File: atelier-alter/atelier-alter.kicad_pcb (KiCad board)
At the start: 2 copper layers, 71.4 x 99.5 mm, 28 parts, among them SW1 SW_Push, U1 ATmega32U4-A, Y1 16Mhz

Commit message: redrawn
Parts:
- added Alter: LOGO, Alter_Drawing, F.Cu at (126.2, 120.7)
- added C10: 100nF, Capacitor_SMD:C_0805_2012Metric, B.Cu at (161.3, 132.6)
- added C11: 100nF, Capacitor_SMD:C_0805_2012Metric, B.Cu at (168.9, 122.1)
- added C8: 100nF, Capacitor_SMD:C_0805_2012Metric, B.Cu at (124.5, 109.5)
- added C9: 100nF, Capacitor_SMD:C_0805_2012Metric, B.Cu at (146.2, 68.3)
- added D10: SK6812, LED_SMD:LED_SK6812_PLCC4_5.0x5.0mm_P3.2mm, B.Cu at (153.2, 111.9)
- added D7: SK6812, LED_SMD:LED_SK6812_PLCC4_5.0x5.0mm_P3.2mm, B.Cu at (127.8, 91.3)
- added D8: SK6812, LED_SMD:LED_SK6812_PLCC4_5.0x5.0mm_P3.2mm, B.Cu at (131.0, 111.9)
- added D9: SK6812, LED_SMD:LED_SK6812_PLCC4_5.0x5.0mm_P3.2mm, B.Cu at (156.4, 91.3)
- added R5: 300, Resistor_SMD:R_0805_2012Metric, B.Cu at (122.4, 68.3)
- C1, C3, C4, C5, C6, D1, D2, D3, D4, D5, D6, R3, U1, Y1: moved to B.Cu
- C2: value C_Small -> 1uF; moved to B.Cu
- C7: value 0.1uF -> 10uF; moved to B.Cu
- R1, R2: value R_Small -> 22
- SW1: value SW_Push -> RESET; moved to B.Cu
- moved R3 52.8 mm to (169.0, 112.7), turned to -90 degrees
- moved F1 49.0 mm to (166.6, 68.3), turned to 180 degrees
- moved SW1 40.9 mm to (161.9, 111.9), turned to 180 degrees
- moved C2 33.4 mm to (161.2, 127.8), turned to 180 degrees
- moved Y1 29.3 mm to (161.6, 122.9), turned to -90 degrees
- moved C1 25.1 mm to (161.4, 118.3), turned to 180 degrees
- moved C5 19.9 mm to (146.9, 111.1), turned to 0 degrees
- moved D5 19.2 mm to (153.2, 79.4), turned to -90 degrees
- moved D1 19.2 mm to (115.1, 79.4), turned to -90 degrees
- moved D3 19.2 mm to (134.1, 79.4), turned to -90 degrees
- moved D4 19.2 mm to (134.1, 98.5), turned to -90 degrees
- moved D6 19.2 mm to (153.2, 98.4), turned to -90 degrees
- moved D2 19.2 mm to (115.1, 98.4), turned to -90 degrees
- moved C6 18.1 mm to (146.9, 113.6), turned to 0 degrees
- moved USB1 16.0 mm to (142.1, 59.8)
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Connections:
- U1 pad 11: unconnected-(U1-Pad11) -> COL1
- U1 pad 27: unconnected-(U1-Pad27) -> ROW1
- U1 pad 28: unconnected-(U1-Pad28) -> COL2
- U1 pad 29: unconnected-(U1-Pad29) -> COL3
- U1 pad 30: unconnected-(U1-Pad30) -> ROW2
- U1 pad 41: unconnected-(U1-Pad41) -> UGLOW1
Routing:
- net UGLOW1: track 0.00 -> 76.9 mm, vias 0 -> 2
- net Net-(R3-Pad1): track 88.5 -> 18.7 mm, vias 0 -> 2
- net ROW1: track 40.0 -> 101.3 mm, vias 3 -> 0
- net ROW2: track 39.8 -> 97.6 mm, vias 3 -> 4
- net COL1: track 19.1 -> 65.6 mm, vias 0 -> 2
- net Net-(D8-Pad4): track 0.00 -> 36.4 mm, vias 0 -> 2
- net Net-(R4-Pad1): track 99.2 -> 67.8 mm, vias 2 -> 3
- net COL2: track 23.9 -> 51.9 mm, vias 0 -> 4
- net Net-(D10-Pad2): track 0.00 -> 25.4 mm, vias 0 -> 2
- net Net-(D7-Pad2): track 0.00 -> 25.1 mm
- net +5V: track 201.1 -> 225.8 mm, vias 6 -> 10
- net Net-(D7-Pad4): track 0.00 -> 19.5 mm
- net Net-(R1-Pad2): track 68.3 -> 52.9 mm, vias 0 -> 1
- net COL3: track 41.9 -> 55.1 mm
- net D-: track 29.6 -> 20.9 mm
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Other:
- board size 71.4 x 99.5 mm -> 61.9 x 78.6 mm
- board text added: "Atelier_Alter_Prototype"
- board text removed: "Atelier_Alter_v0.1"

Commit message: da route thu nghiem xong xuoi
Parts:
- R5: moved to F.Cu
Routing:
- net ROW1: track 101.3 -> 141.4 mm, vias 0 -> 5
- net ROW2: track 97.6 -> 117.9 mm, vias 4 -> 6
- net COL3: track 55.1 -> 74.8 mm, vias 0 -> 2
- net +5V: track 225.8 -> 228.4 mm
- net COL2: track 51.9 -> 53.5 mm
- net Net-(R4-Pad1): track 67.8 -> 68.9 mm
- net GND: track 224.0 -> 224.9 mm
- net COL1: track 65.6 -> 66.3 mm
- net UGLOW1: track 76.9 -> 76.3 mm, vias 2 -> 1
- net Net-(D7-Pad2): vias 0 -> 1

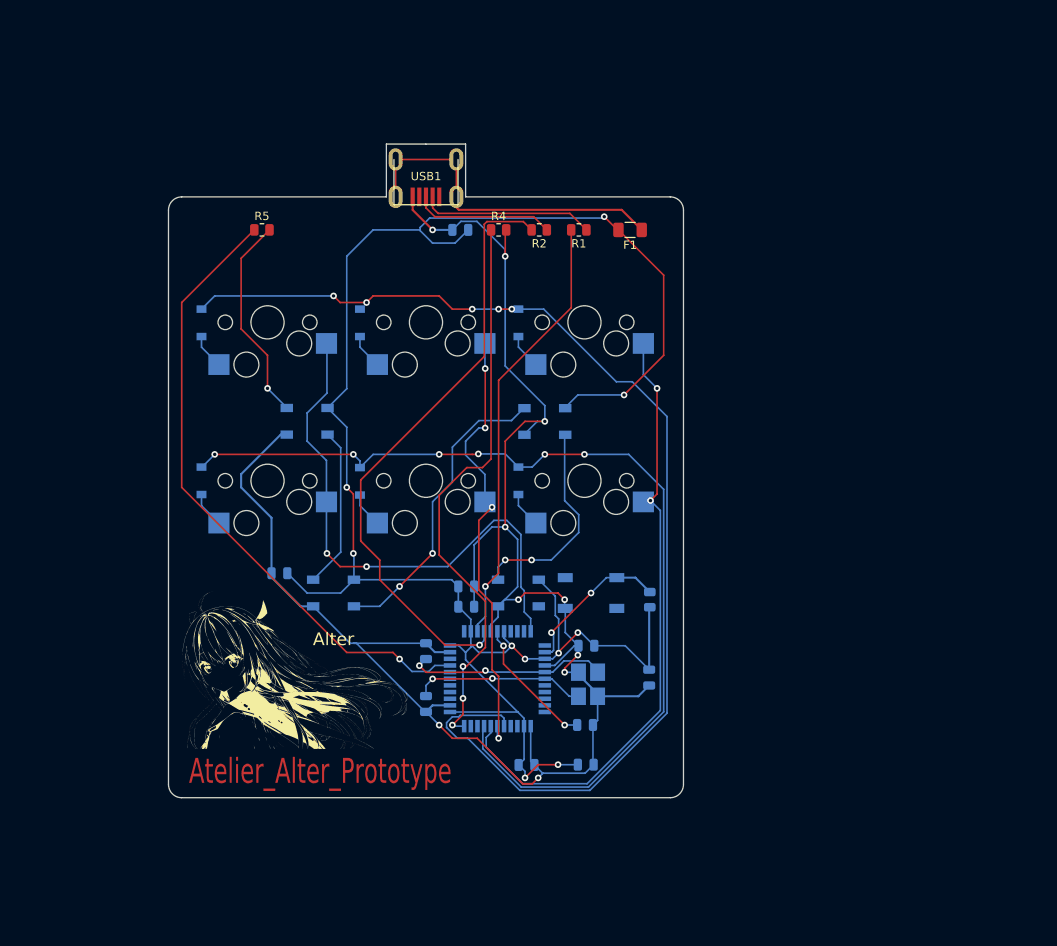
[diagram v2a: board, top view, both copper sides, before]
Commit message: redrawn lan 3, them vai chuc nang
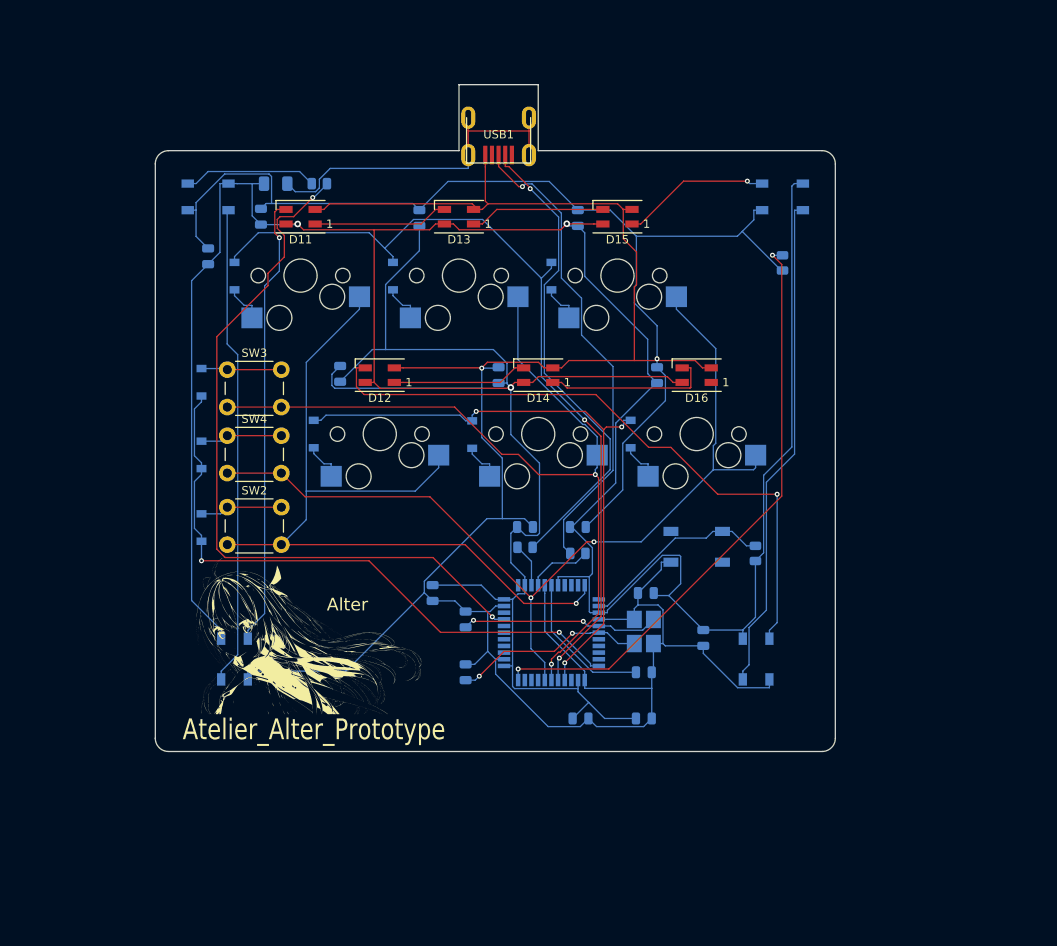
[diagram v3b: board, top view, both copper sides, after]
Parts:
- added C12: 100uF, Capacitor_SMD:C_0805_2012Metric, B.Cu at (122.2, 66.7)
- added C13: 100uF, Capacitor_SMD:C_0805_2012Metric, B.Cu at (131.8, 85.6)
- added C14: 100uF, Capacitor_SMD:C_0805_2012Metric, B.Cu at (141.3, 66.8)
- added C15: 100uF, Capacitor_SMD:C_0805_2012Metric, B.Cu at (150.8, 85.7)
- added C16: 100uF, Capacitor_SMD:C_0805_2012Metric, B.Cu at (160.3, 66.8)
- added C17: 100uF, Capacitor_SMD:C_0805_2012Metric, B.Cu at (169.9, 85.7)
- added D11: SK6812MINI, LED_SMD:LED_SK6812MINI_PLCC4_3.5x3.5mm_P1.75mm, F.Cu at (127.0, 66.7)
- added D12: SK6812MINI, LED_SMD:LED_SK6812MINI_PLCC4_3.5x3.5mm_P1.75mm, F.Cu at (136.5, 85.7)
- added D13: SK6812MINI, LED_SMD:LED_SK6812MINI_PLCC4_3.5x3.5mm_P1.75mm, F.Cu at (146.1, 66.7)
- added D14: SK6812MINI, LED_SMD:LED_SK6812MINI_PLCC4_3.5x3.5mm_P1.75mm, F.Cu at (155.6, 85.7)
- added D15: SK6812MINI, LED_SMD:LED_SK6812MINI_PLCC4_3.5x3.5mm_P1.75mm, F.Cu at (165.1, 66.7)
- added D16: SK6812MINI, LED_SMD:LED_SK6812MINI_PLCC4_3.5x3.5mm_P1.75mm, F.Cu at (174.6, 85.7)
- added D17: SOD-123, Diode_SMD:D_SOD-123, B.Cu at (115.1, 104.0)
- added D18: SOD-123, Diode_SMD:D_SOD-123, B.Cu at (115.1, 86.6)
- added D19: SOD-123, Diode_SMD:D_SOD-123, B.Cu at (115.1, 95.3)
- added SW2: SW_DPST, Button_Switch_THT:SW_PUSH_6mm_H9.5mm, F.Cu at (118.2, 101.6)
- added SW3: SW_DPST, Button_Switch_THT:SW_PUSH_6mm_H9.5mm, F.Cu at (118.2, 85.1)
- added SW4: SW_DPST, Button_Switch_THT:SW_PUSH_6mm_H9.5mm, F.Cu at (118.2, 93.0)
- D1, D2, D3, D4, D5, D6: value D_Small -> SOD-123
- F1, R1, R2, R4, R5: moved to B.Cu
- moved C9 43.8 mm to (142.9, 111.9), turned to -90 degrees
- moved F1 43.0 mm to (124.0, 62.7)
- moved D9 39.3 mm to (184.9, 64.3)
- moved R2 39.2 mm to (160.3, 107.2), turned to 0 degrees
- moved C8 39.1 mm to (115.9, 71.4), turned to 90 degrees
- moved R1 38.7 mm to (154.0, 106.4)
- moved R4 34.4 mm to (184.9, 72.2), turned to -90 degrees
- moved D10 29.7 mm to (181.8, 119.9), turned to -90 degrees
- moved D7 29.5 mm to (115.9, 64.3)
- moved C6 16.5 mm to (160.3, 104.0)
- moved D2 14.6 mm to (128.6, 92.8)
- moved D6 14.6 mm to (166.7, 92.8)
- moved MX2 14.6 mm to (136.5, 92.8)
- moved MX6 14.6 mm to (174.6, 92.8)
- moved D4 14.6 mm to (147.6, 92.9)
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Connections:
- net UGLOW1 renamed RGB
- D10 pad 4: unconnected-(D10-Pad4) -> D21
- D8 pad 4: Net-(D8-Pad4) -> D11
- D9 pad 2: Net-(D8-Pad4) -> D12
- U1 pad 22: unconnected-(U1-Pad22) -> ROW3
- U1 pad 26: unconnected-(U1-Pad26) -> ROW2
- U1 pad 30: ROW2 -> unconnected-(U1-Pad30)
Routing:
- net GND: track 224.9 -> 441.6 mm, vias 10 -> 2
- net +5V: track 228.4 -> 440.4 mm, vias 10 -> 3
- net D21: track 0.00 -> 77.0 mm, vias 0 -> 1
- net ROW3: track 0.00 -> 74.4 mm, vias 0 -> 2
- net Net-(R2-Pad2): track 73.2 -> 7.86 mm, vias 1 -> 0
- net D11: track 0.00 -> 54.6 mm, vias 0 -> 1
- net Net-(R1-Pad2): track 52.9 -> 5.26 mm, vias 1 -> 0
- net COL2: track 53.5 -> 100.5 mm, vias 4 -> 2
- net ROW2: track 117.9 -> 73.3 mm, vias 6 -> 3
- net D+: track 16.9 -> 57.8 mm, vias 0 -> 1
- net ROW1: track 141.4 -> 101.8 mm, vias 5 -> 2
- net Net-(D7-Pad4): track 19.5 -> 57.8 mm
- net D-: track 20.9 -> 57.9 mm, vias 0 -> 1
- net Net-(D8-Pad4): track 36.4 -> 0.00 mm, vias 2 -> 0
- net COL3: track 74.8 -> 111.2 mm
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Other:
- board size 61.9 x 78.6 mm -> 81.8 x 80.2 mm

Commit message: kaka, rat manh
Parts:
- added R6: 5.1k, Capacitor_SMD:C_0805_2012Metric, B.Cu at (138.6, 62.7)
- added R7: 5.1k, Capacitor_SMD:C_0805_2012Metric, B.Cu at (134.1, 62.7)
- added U2: PRTR5V0U2X, Package_TO_SOT_SMD:SOT-143_Handsoldering, F.Cu at (178.6, 71.3)
- USB1: value Molex-0548190519 -> HRO-TYPE-C-31-M-12; footprint random-keyboard-parts:Molex-0548190589 -> Type-C:HRO-TYPE-C-31-M-12-HandSoldering
- moved C9 19.2 mm to (125.4, 119.9), turned to 90 degrees
- moved USB1 3.97 mm to (150.8, 50.8), turned to 180 degrees
- moved R4 3.17 mm to (184.9, 69.1), turned to 180 degrees
- moved C11 2.66 mm to (176.2, 119.9)
- moved R1 0.73 mm to (154.0, 107.2)
- turned C12 to 90 degrees
- turned C13 to 90 degrees
- turned C14 to 90 degrees
- turned C15 to 90 degrees
- turned C16 to 90 degrees
- turned C17 to 90 degrees
- turned D10 to 180 degrees
- turned D11 to 0 degrees
- turned D12 to 0 degrees
- turned D13 to 0 degrees
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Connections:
- U1 pad 11: COL1 -> unconnected-(U1-Pad11)
- U1 pad 18: unconnected-(U1-Pad18) -> RGB
- U1 pad 19: unconnected-(U1-Pad19) -> COL1
- U1 pad 20: unconnected-(U1-Pad20) -> COL2
- U1 pad 21: unconnected-(U1-Pad21) -> COL3
- U1 pad 28: COL2 -> unconnected-(U1-Pad28)
- U1 pad 29: COL3 -> unconnected-(U1-Pad29)
- U1 pad 41: RGB -> unconnected-(U1-Pad41)
- USB1 pad 2: unconnected-(USB1-Pad2) -> +5V
- USB1 pad 3: D+ -> unconnected-(USB1-Pad3)
- USB1 pad 4: D- -> Net-(R6-Pad2)
- USB1 pad 5: unconnected-(USB1-Pad5) -> D-
- USB1 pad 6: VCC -> D+
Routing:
- net GND: track 441.6 -> 0.00 mm, vias 2 -> 0
- net VCC: track 41.8 -> 0.00 mm
- net D+: track 57.8 -> 87.4 mm
- net D-: track 57.9 -> 86.9 mm
- net +5V: track 440.4 -> 460.9 mm, vias 3 -> 1
- net Net-(R7-Pad2): track 0.00 -> 19.0 mm, vias 0 -> 1
- net Net-(R6-Pad2): track 0.00 -> 16.2 mm, vias 0 -> 1
- net COL3: track 111.2 -> 124.3 mm
- net RGB: track 89.2 -> 76.1 mm
- net COL1: track 99.8 -> 86.9 mm, vias 1 -> 2
- net COL2: track 100.5 -> 87.8 mm, vias 2 -> 3
- net D21: track 77.0 -> 84.7 mm
- net Net-(D7-Pad4): track 57.8 -> 65.3 mm
- net ROW1: track 101.8 -> 109.0 mm, vias 2 -> 0
- net Net-(D13-Pad1): track 16.3 -> 23.3 mm, vias 0 -> 2
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- added copper zone on B.Cu, net GND
- added copper zone on F.Cu, net GND
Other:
- outline, holes or cut-outs redrawn

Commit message: add essentials
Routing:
- net D21: track 84.7 -> 62.5 mm
- net +5V: track 460.9 -> 482.4 mm
- net RGB: track 76.1 -> 96.9 mm
- net COL1: track 86.9 -> 99.2 mm, vias 2 -> 1
- net ROW2: track 75.7 -> 86.9 mm, vias 3 -> 2
- net COL2: track 87.8 -> 97.2 mm, vias 3 -> 2
- net COL3: track 124.3 -> 115.8 mm, vias 2 -> 1
- net D+: track 87.4 -> 80.1 mm
- net Net-(D7-Pad4): track 65.3 -> 60.9 mm
- net ROW1: track 109.0 -> 104.7 mm
- net Net-(D10-Pad2): track 60.9 -> 57.1 mm
- net Net-(C4-Pad2): track 25.6 -> 29.2 mm, vias 2 -> 0
- net Net-(R4-Pad1): track 73.7 -> 76.9 mm, vias 2 -> 0
- net D-: track 86.9 -> 88.4 mm
- net Net-(D17-Pad2): track 11.3 -> 9.93 mm, vias 1 -> 0
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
